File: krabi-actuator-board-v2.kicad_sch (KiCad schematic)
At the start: 47 parts, among them J1 Power, J2 PWM, J3 Analog, J4 PWM, J5 Analog, J6 Communication, J7 Digital, J8 Conn_01x02_Pin, U1 XGZP6897D_differential_pressu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, U2 XGZP6897D_differential_pressu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

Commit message: adding LED strip
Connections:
- net 35 renamed LEDS_1
- net 37 renamed LEDS_2
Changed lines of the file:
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@@
+    )
+  )
+  (global_label "LEDS_2" (shape output) (at 52.07 156.21 270) (fields_autoplaced)
+    (effects (font (size 1.27 1.27)) (justify right))
+    (property "Intersheetrefs" "${INTERSHEET_REFS}" (at 52.07 166.124 90)
+      (effects (font (size 1.27 1.27)) (justify right) hide)
     )
   )
@@
     (property "Intersheetrefs" "${INTERSHEET_REFS}" (at 155.1779 22.86 0)
       (effects (font (size 1.27 1.27)) (justify left) hide)
+    )
+  )
+  (global_label "LEDS_1" (shape output) (at 54.61 156.21 270) (fields_autoplaced)
+    (effects (font (size 1.27 1.27)) (justify right))
+    (property "Intersheetrefs" "${INTERSHEET_REFS}" (at 54.61 166.124 90)
+      (effects (font (size 1.27 1.27)) (justify right) hide)
     )
   )
@@
     )
   )
-  (sheet (at 129.54 179.07) (size 34.29 10.16) (fields_autoplaced)
+  (sheet (at 137.16 83.82) (size 34.29 10.16) (fields_autoplaced)
     (stroke (width 0.1524) (type solid))
     (fill (color 0 0 0 0.0000))
-    (property "Sheetname" "servos" (at 129.54 178.3584 0)
+    (property "Sheetname" "servos" (at 137.16 83.1084 0)
       (effects (font (size 1.27 1.27)) (justify left bottom))
     )
-    (property "Sheetfile" "krabi-actuator-board-servos.kicad_sch" (at 129.54 189.8146 0)
+    (property "Sheetfile" "krabi-actuator-board-servos.kicad_sch" (at 137.16 94.5646 0)
       (effects (font (size 1.27 1.27)) (justify left top))
     )

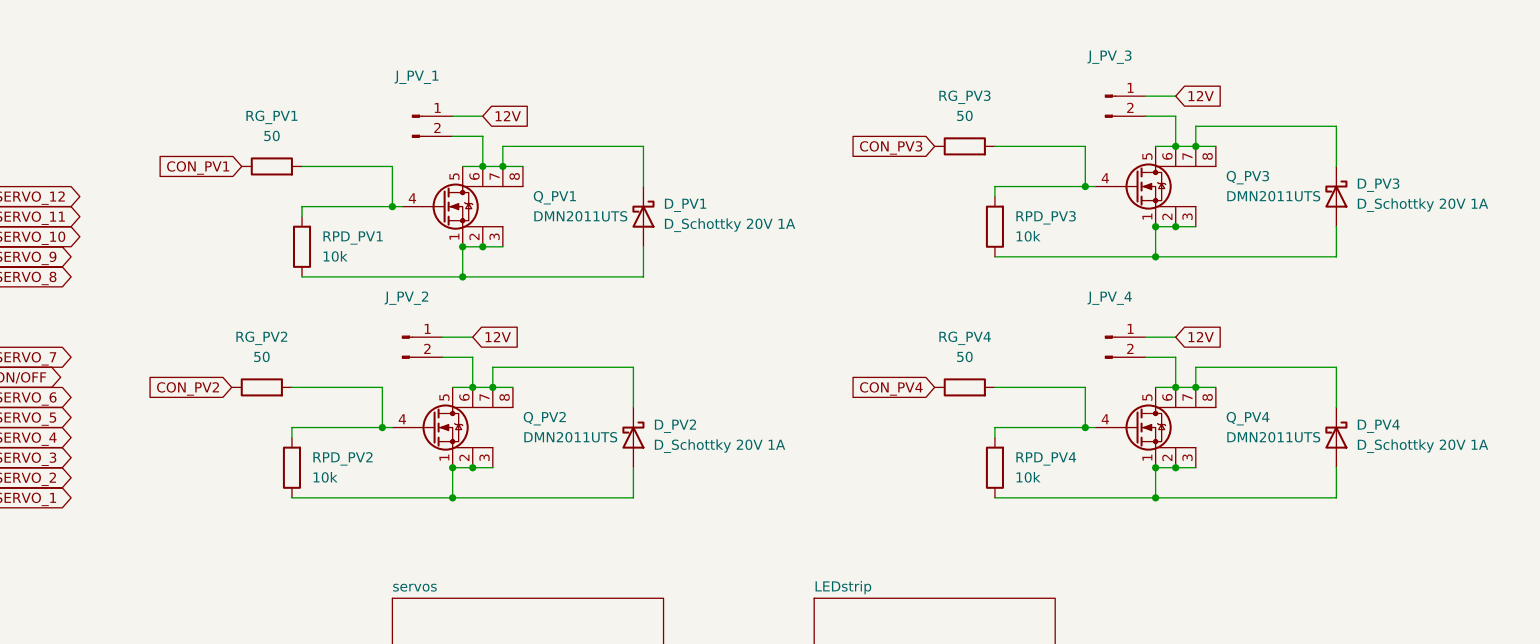
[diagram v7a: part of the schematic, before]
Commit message: Add 2 led strip & led visualisation on all outputs
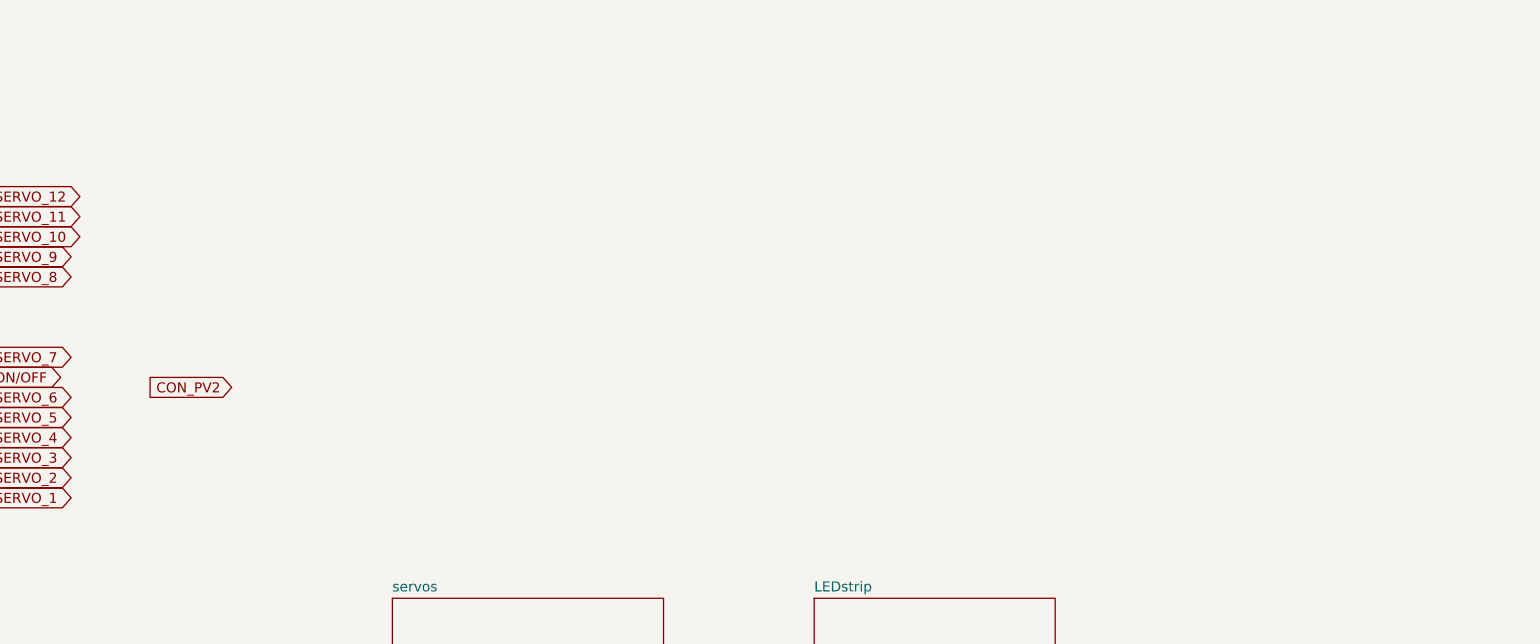
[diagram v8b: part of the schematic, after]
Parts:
- removed D_PV1, D_PV2, D_PV3, D_PV4: D_Schottky 20V 1A, symbol Device:D_Schottky
- removed J_PV_1, J_PV_2, J_PV_3, J_PV_4: ~, symbol Connector:Conn_01x02_Pin
- removed Q_PV1, Q_PV2, Q_PV3, Q_PV4: DMN2011UTS, Package_SO:TSSOP-8_4.4x3mm_P0.65mm, symbol Krabi:DMN2011UTS
- removed RG_PV1, RG_PV2, RG_PV3, RG_PV4: 50, symbol Device:R
- removed RPD_PV1, RPD_PV2, RPD_PV3, RPD_PV4: 10k, symbol Device:R
